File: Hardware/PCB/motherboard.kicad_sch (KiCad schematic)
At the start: 0 parts

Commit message: added stm32 to the project
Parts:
- added C8: 0.1 uF, symbol Device:C
- added JP1: Jumper, symbol Jumper:SolderJumper_2_Open
- added P1: USB_C_Plug_USB2.0, symbol Connector:USB_C_Plug_USB2.0
- added SW1: reset btn, symbol Switch:SW_Push
- added U4: STM32F303VCTx, Package_QFP:LQFP-100_14x14mm_P0.5mm, symbol MCU_ST_STM32F3:STM32F303VCTx
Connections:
- new net: C8.1, SW1.2, U4.14 (NRST)
- new net +3.3V: JP1.1 (A), U4.94 (BOOT0)
- new net GND: C8.2, JP1.2 (B), P1.A1 (GND), P1.A12 (GND), P1.B1 (GND), P1.B12 (GND), P1.SH (SHIELD), SW1.1, U4.20 (VSSA), U4.49 (VSS), U4.74 (VSS), U4.99 (VSS)
- new net USB_D+: P1.A6 (D+), U4.71 (PA12)
- new net USB_D-: P1.A7 (D-), U4.70 (PA11)
- new net VBUS: P1.A4 (VBUS), P1.A9 (VBUS), P1.B4 (VBUS), P1.B9 (VBUS)
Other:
- title: (none) -> STM32 mothersheet

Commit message: adding power management
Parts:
- removed P1: USB_C_Plug_USB2.0, symbol Connector:USB_C_Plug_USB2.0
- added C13, C14: 470n, symbol Device:C
- added C16, C17, C18, C3: 100n, symbol Device:C
- added C19, C21: 100n, Capacitor_SMD:C_0402_1005Metric, symbol Device:C
- added C2: 10u, symbol Device:C
- added C20: 4.7u, symbol Device:C
- added C4, C5: 22u, symbol Device:C
- added J1: USB4105-GF-A, Connector_USB:USB_C_Receptacle_GCT_USB4105-xx-A_16P_TopMnt_Horizontal, symbol Connector:USB_C_Receptacle_USB2.0_16P
- added L1: 3.9u, symbol Device:L
- added R14: 0R, symbol Device:R
- added R15, R16: 5K1, symbol Device:R
- added TP1: USB D1-, symbol Connector:TestPoint
- added TP2: USB D1+, symbol Connector:TestPoint
- added TP3: Vbus, symbol Connector:TestPoint
- added TP4: 3.3V, symbol Connector:TestPoint
- added U2: AP63203WU, Package_TO_SOT_SMD:TSOT-23-6, symbol Regulator_Switching:AP63203WU
- JP1: footprint (none) -> Jumper:SolderJumper-2_P1.3mm_Open_RoundedPad1.0x1.5mm
- renumbered C8 to C1, U4 to U1
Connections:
- net +3.3V: now also U1.100 (VDD), U1.21 (VREF+), U1.22 (VDDA), U1.28 (VDD), U1.50 (VDD), U1.75 (VDD), C16.1, C17.1, C18.1, C19.1, C20.1, C21.1, C4.1, C5.2, L1.2, TP4.1, U2.1 (FB)
- net GND: now also C13.2, C14.2, C16.2, C17.2, C18.2, C19.2, C2.2, C20.2, C21.2, C4.2, C5.1, J1.A1 (GND), J1.A12 (GND), J1.B1 (GND), J1.B12 (GND), J1.SH (SHIELD), R15.2, R16.2, U2.4 (GND)
- net USB_D+: now also J1.A6 (D+), J1.B6 (D+), TP2.1
- net USB_D-: now also J1.A7 (D-), J1.B7 (D-), TP1.1
- net VBUS: now also C13.1, C2.1, J1.A4 (VBUS), J1.A9 (VBUS), J1.B4 (VBUS), J1.B9 (VBUS), R14.2, TP3.1, U2.2 (EN), U2.3 (IN)
- new net: C3.1, U2.6 (BST)
- new net: C3.2, L1.1, U2.5 (SW)
- new net: J1.A5 (CC1), R15.1
- new net: J1.B5 (CC2), R16.1
- new net: C14.1, R14.1
- no-connect marks 0 -> 2
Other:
- note added: "Buck IC 5V->3.3V"
- note added: "PI filter"
- note added: "USB4105-GF-A"
- note added: "jlc link"
- note added: "must be connected to VDDA"
- note added: "voltage testpoints"

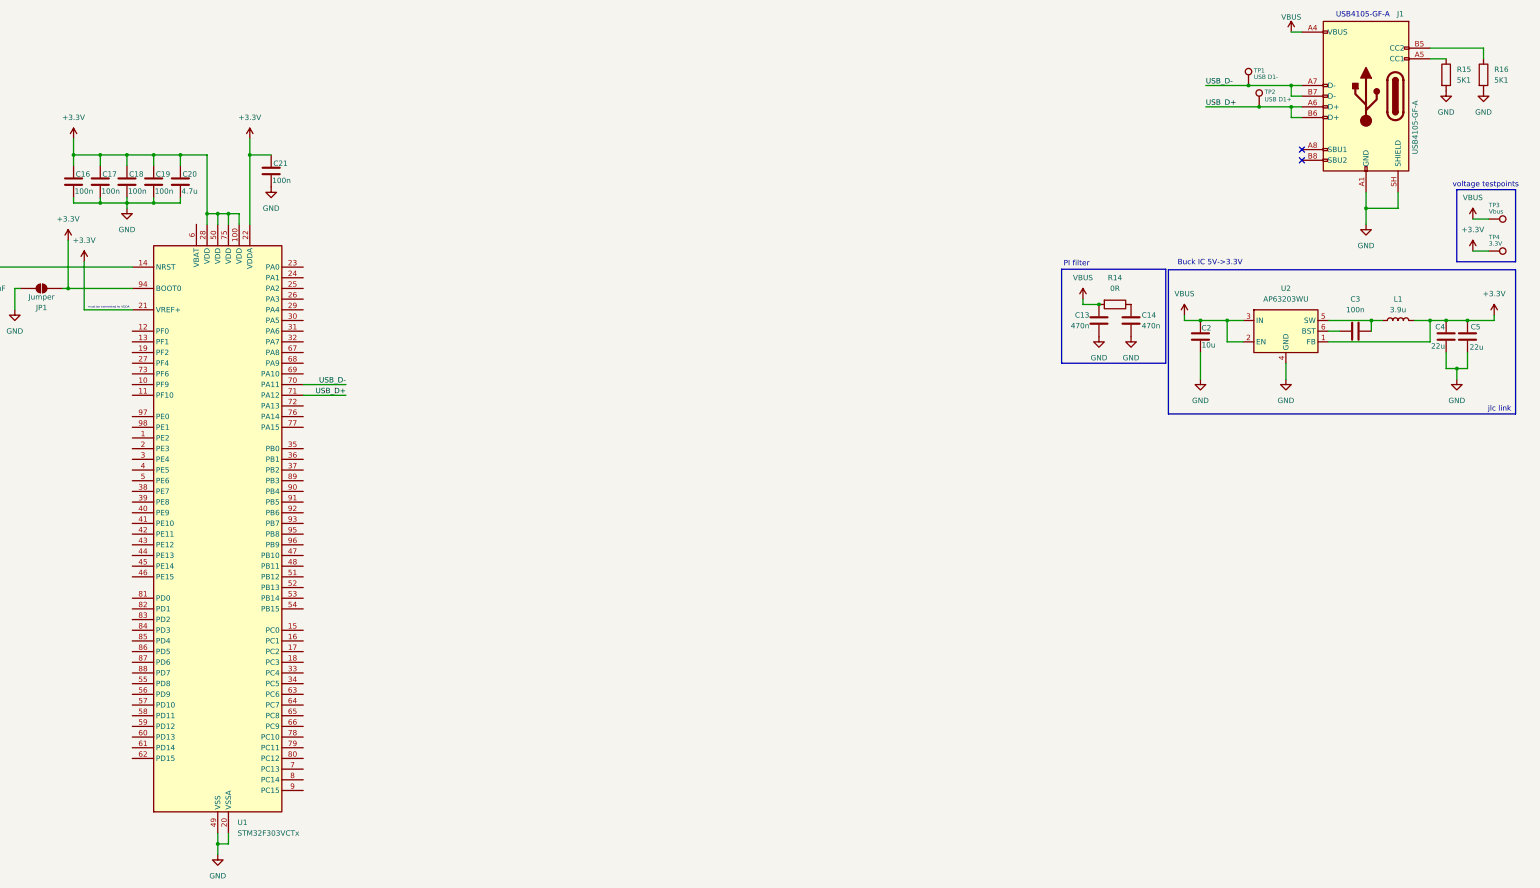
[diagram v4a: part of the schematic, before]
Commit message: added status LED's esd protection and new RGB symbol
Mass renumbering and library updates across KiCad schematics: updated many component Reference fields in Hardware/PCB/FM_reciever.kicad_sch and adjusted the project used_designators in Radiowekker.kicad_pro to match. Added a Device:LED symbol (with LED variants) to motherboard.kicad_sch and replaced the AP63203WU regulator symbol with a USBLC6-2SC6 power-protection symbol (updated footprint, datasheet, pins and graphics). Also added sym-lib-table and an RGB_leds symbol library. These changes keep designators consistent and introduce LED/ESD protection symbols for use in the PCB designs.
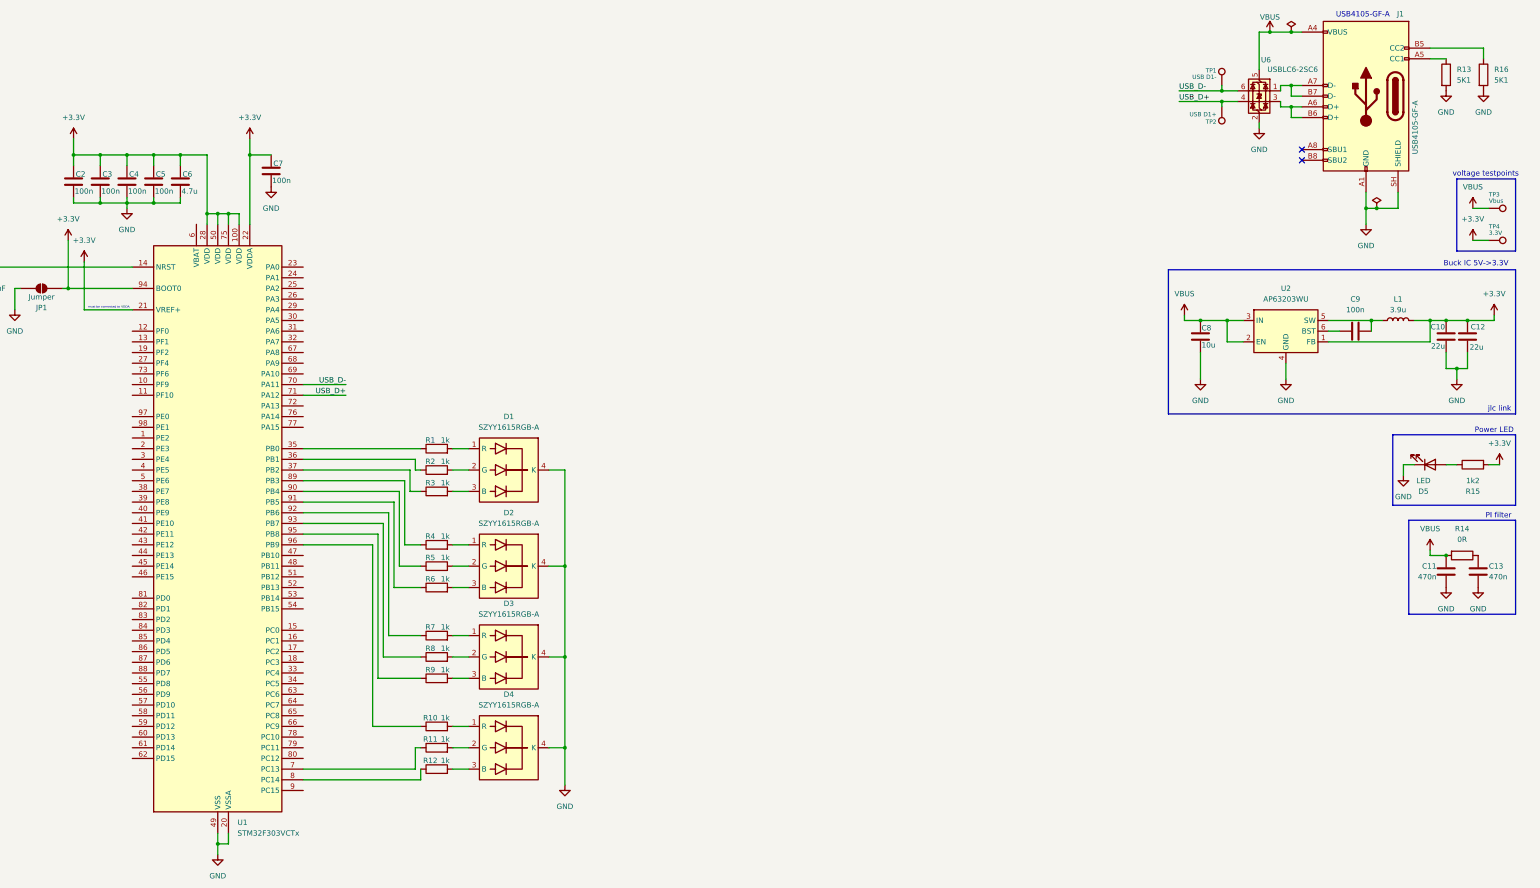
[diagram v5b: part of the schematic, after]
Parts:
- added D1, D2, D3, D4: SZYY1615RGB-A, symbol RGB_leds:SZYY1615RGB-A
- added D5: LED, symbol Device:LED
- added R1, R10, R11, R12, R2, R3, R4, R5, R6, R7, R8, R9: 1k, symbol Device:R
- added R15: 1k2, symbol Device:R
- added U6: USBLC6-2SC6, Package_TO_SOT_SMD:SOT-23-6, symbol Power_Protection:USBLC6-2SC6
- renumbered C4 to C10, C13 to C11, C5 to C12, C14 to C13, C16 to C2, C17 to C3, C18 to C4, C19 to C5, C20 to C6, C21 to C7, C2 to C8, C3 to C9, R15 to R13
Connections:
- net +3.3V: now also R15.2
- net GND: now also D1.4 (K), D2.4 (K), D3.4 (K), D4.4 (K), D5.1 (K), U6.2 (GND)
- net USB_D+: now also U6.4 (I/O2); no longer J1.A6 (D+), J1.B6 (D+)
- net USB_D-: now also U6.6 (I/O1); no longer J1.A7 (D-), J1.B7 (D-)
- net VBUS: now also U6.5 (VBUS)
- net at U1.35 (PB0): now also R1.1
- net at U1.36 (PB1): now also R2.1
- net at U1.37 (PB2): now also R3.1
- net at U1.7 (PC13): now also R11.1
- net at U1.8 (PC14): now also R12.1
- net at U1.89 (PB3): now also R4.1
- net at U1.90 (PB4): now also R5.1
- net at U1.91 (PB5): now also R6.1
- net at U1.92 (PB6): now also R7.1
- net at U1.93 (PB7): now also R8.1
- net at U1.95 (PB8): now also R9.1
- net at U1.96 (PB9): now also R10.1
- new net: D1.1 (R), R1.2
- new net: D3.2 (G), R8.2
- new net: D3.3 (B), R9.2
- new net: D1.2 (G), R2.2
- new net: D4.2 (G), R11.2
- new net: D3.1 (R), R7.2
- new net: D4.1 (R), R10.2
- new net: D4.3 (B), R12.2
- new net: D2.3 (B), R6.2
- new net: D2.1 (R), R4.2
- new net: D2.2 (G), R5.2
- new net: J1.A7 (D-), J1.B7 (D-), U6.1 (I/O1)
- new net: J1.A6 (D+), J1.B6 (D+), U6.3 (I/O2)
- new net: D1.3 (B), R3.2
- new net: D5.2 (A), R15.1
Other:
- note added: "Power LED"
- moved on the sheet: C11, C13, R14, TP1, TP2, TP3, TP4

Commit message: added UI
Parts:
- renumbered U6 to U2, U2 to U3
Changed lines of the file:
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@@
 		(dnp no)
 		(fields_autoplaced yes)
-		(property "Reference" "#PWR020"
+		(property "Reference" "#PWR021"
 			(at 544.83 163.83 0)
 			(hide yes)
@@
 			(project "Radiowekker"
 				(path "/d1c96533-fea5-409f-9018-c843faf96bf8/031f395c-467c-47af-acd6-d1b5a436666d"
-					(reference "#PWR020")
+					(reference "#PWR021")
 					(unit 1)
 				)
@@
 		(dnp no)
 		(fields_autoplaced yes)
-		(property "Reference" "#PWR026"
+		(property "Reference" "#PWR027"
 			(at 556.26 96.52 0)
 			(hide yes)
@@
 			(project "Radiowekker"
 				(path "/d1c96533-fea5-409f-9018-c843faf96bf8/031f395c-467c-47af-acd6-d1b5a436666d"
-					(reference "#PWR026")
+					(reference "#PWR027")
 					(unit 1)
 				)
@@
 		(dnp no)
 		(fields_autoplaced yes)
-		(property "Reference" "#PWR024"
+		(property "Reference" "#PWR025"
 			(at 552.45 163.83 0)
 			(hide yes)
@@
 			(project "Radiowekker"
 				(path "/d1c96533-fea5-409f-9018-c843faf96bf8/031f395c-467c-47af-acd6-d1b5a436666d"
-					(reference "#PWR024")
+					(reference "#PWR025")
 					(unit 1)
 				)
@@
 		(in_pos_files yes)
 		(dnp no)
-		(property "Reference" "#PWR014"
+		(property "Reference" "#PWR015"
 			(at 502.92 29.21 0)
 			(hide yes)
@@
 			(project "Radiowekker"
 				(path "/d1c96533-fea5-409f-9018-c843faf96bf8/031f395c-467c-47af-acd6-d1b5a436666d"
-					(reference "#PWR014")
+					(reference "#PWR015")
 					(unit 1)
 				)
@@
 		(dnp no)
 		(fields_autoplaced yes)
-		(property "Reference" "#PWR027"
+		(property "Reference" "#PWR028"
 			(at 557.53 132.08 0)
 			(hide yes)
@@
 			(project "Radiowekker"
 				(path "/d1c96533-fea5-409f-9018-c843faf96bf8/031f395c-467c-47af-acd6-d1b5a436666d"
-					(reference "#PWR027")
+					(reference "#PWR028")
 					(unit 1)
 				)
@@
 		(dnp no)
 		(fields_autoplaced yes)
-		(property "Reference" "#PWR016"
+		(property "Reference" "#PWR017"
 			(at 525.78 77.47 0)
 			(hide yes)
@@
 			(project "Radiowekker"
 				(path "/d1c96533-fea5-409f-9018-c843faf96bf8/031f395c-467c-47af-acd6-d1b5a436666d"
-					(reference "#PWR016")
+					(reference "#PWR017")
 					(unit 1)
 				)
@@
 		(dnp no)
 		(fields_autoplaced yes)
-		(property "Reference" "#PWR018"
+		(property "Reference" "#PWR019"
 			(at 541.02 152.4 0)
 			(hide yes)
@@
 			(project "Radiowekker"
 				(path "/d1c96533-fea5-409f-9018-c843faf96bf8/031f395c-467c-47af-acd6-d1b5a436666d"
-					(reference "#PWR018")
+					(reference "#PWR019")
 					(unit 1)
 				)
@@
 		(in_pos_files yes)
 		(dnp no)
-		(property "Reference" "U6"
+		(property "Reference" "U2"
 			(at 503.174 32.004 0)
 			(show_name no)
@@
 			(project "Radiowekker"
 				(path "/d1c96533-fea5-409f-9018-c843faf96bf8/031f395c-467c-47af-acd6-d1b5a436666d"
-					(reference "U6")
+					(reference "U2")
 					(unit 1)
 				)
@@
 		(dnp no)
 		(fields_autoplaced yes)
-		(property "Reference" "#PWR025"
+		(property "Reference" "#PWR026"
 			(at 553.72 45.72 0)
 			(hide yes)
@@
 			(project "Radiowekker"
 				(path "/d1c96533-fea5-409f-9018-c843faf96bf8/031f395c-467c-47af-acd6-d1b5a436666d"
-					(reference "#PWR025")
+					(reference "#PWR026")
 					(unit 1)
 				)
@@
 		(dnp no)
 		(fields_autoplaced yes)
-		(property "Reference" "#PWR022"
+		(property "Reference" "#PWR023"
 			(at 551.18 71.12 0)
 			(hide yes)
@@
 			(project "Radiowekker"
 				(path "/d1c96533-fea5-409f-9018-c843faf96bf8/031f395c-467c-47af-acd6-d1b5a436666d"
-					(reference "#PWR022")
+					(reference "#PWR023")
 					(unit 1)
 				)
@@
 		(dnp no)
 		(fields_autoplaced yes)
-		(property "Reference" "#PWR019"
+		(property "Reference" "#PWR020"
 			(at 544.83 45.72 0)
 			(hide yes)
@@
 			(project "Radiowekker"
 				(path "/d1c96533-fea5-409f-9018-c843faf96bf8/031f395c-467c-47af-acd6-d1b5a436666d"
-					(reference "#PWR019")
+					(reference "#PWR020")
 					(unit 1)
 				)
@@
 		(dnp no)
 		(fields_autoplaced yes)
-		(property "Reference" "#PWR023"
+		(property "Reference" "#PWR024"
 			(at 551.18 78.74 0)
 			(hide yes)
@@
 			(project "Radiowekker"
 				(path "/d1c96533-fea5-409f-9018-c843faf96bf8/031f395c-467c-47af-acd6-d1b5a436666d"
-					(reference "#PWR023")
+					(reference "#PWR024")
 					(unit 1)
 				)
@@
 		(dnp no)
 		(fields_autoplaced yes)
-		(property "Reference" "#PWR041"
+		(property "Reference" "#PWR014"
 			(at 500.38 54.61 0)
 			(hide yes)
@@
 			(project "Radiowekker"
 				(path "/d1c96533-fea5-409f-9018-c843faf96bf8/031f395c-467c-47af-acd6-d1b5a436666d"
-					(reference "#PWR041")
+					(reference "#PWR014")
 					(unit 1)
 				)
@@
 		(dnp no)
 		(fields_autoplaced yes)
-		(property "Reference" "#PWR021"
+		(property "Reference" "#PWR022"
 			(at 547.37 114.3 0)
 			(hide yes)
@@
 			(project "Radiowekker"
 				(path "/d1c96533-fea5-409f-9018-c843faf96bf8/031f395c-467c-47af-acd6-d1b5a436666d"
-					(reference "#PWR021")
+					(reference "#PWR022")
 					(unit 1)
 				)
@@
 		(dnp no)
 		(fields_autoplaced yes)
-		(property "Reference" "#PWR017"
+		(property "Reference" "#PWR018"
 			(at 534.67 137.16 0)
 			(hide yes)
@@
 			(project "Radiowekker"
 				(path "/d1c96533-fea5-409f-9018-c843faf96bf8/031f395c-467c-47af-acd6-d1b5a436666d"
-					(reference "#PWR017")
+					(reference "#PWR018")
 					(unit 1)
 				)
@@
 		(dnp no)
 		(fields_autoplaced yes)
-		(property "Reference" "U2"
+		(property "Reference" "U3"
 			(at 506.73 86.36 0)
 			(show_name no)
@@
 			(project "Radiowekker"
 				(path "/d1c96533-fea5-409f-9018-c843faf96bf8/031f395c-467c-47af-acd6-d1b5a436666d"
-					(reference "U2")
+					(reference "U3")
 					(unit 1)
 				)
@@
 		(dnp no)
 		(fields_autoplaced yes)
-		(property "Reference" "#PWR015"
+		(property "Reference" "#PWR016"
 			(at 506.73 114.3 0)
 			(hide yes)
@@
 			(project "Radiowekker"
 				(path "/d1c96533-fea5-409f-9018-c843faf96bf8/031f395c-467c-47af-acd6-d1b5a436666d"
-					(reference "#PWR015")
+					(reference "#PWR016")
 					(unit 1)
 				)

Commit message: added buttons
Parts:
- removed C10, C12: 22u, symbol Device:C
- removed C11, C13: 470n, symbol Device:C
- removed C8: 10u, symbol Device:C
- removed C9: 100n, symbol Device:C
- removed D5: LED, symbol Device:LED
- removed L1: 3.9u, symbol Device:L
- removed R14: 0R, symbol Device:R
- removed R15: 1k2, symbol Device:R
- removed TP3: Vbus, symbol Connector:TestPoint
- removed TP4: 3.3V, symbol Connector:TestPoint
- removed U3: AP63203WU, Package_TO_SOT_SMD:TSOT-23-6, symbol Regulator_Switching:AP63203WU
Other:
- note added: "STM32 IC"
- note added: "USB C connector"
- note removed: "Buck IC 5V->3.3V"
- note removed: "PI filter"
- note removed: "Power LED"
- note removed: "jlc link"
- note removed: "voltage testpoints"
- moved on the sheet: C1, C2, C3, C4, C5, C6, C7, D1, D2, D3, D4, J1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

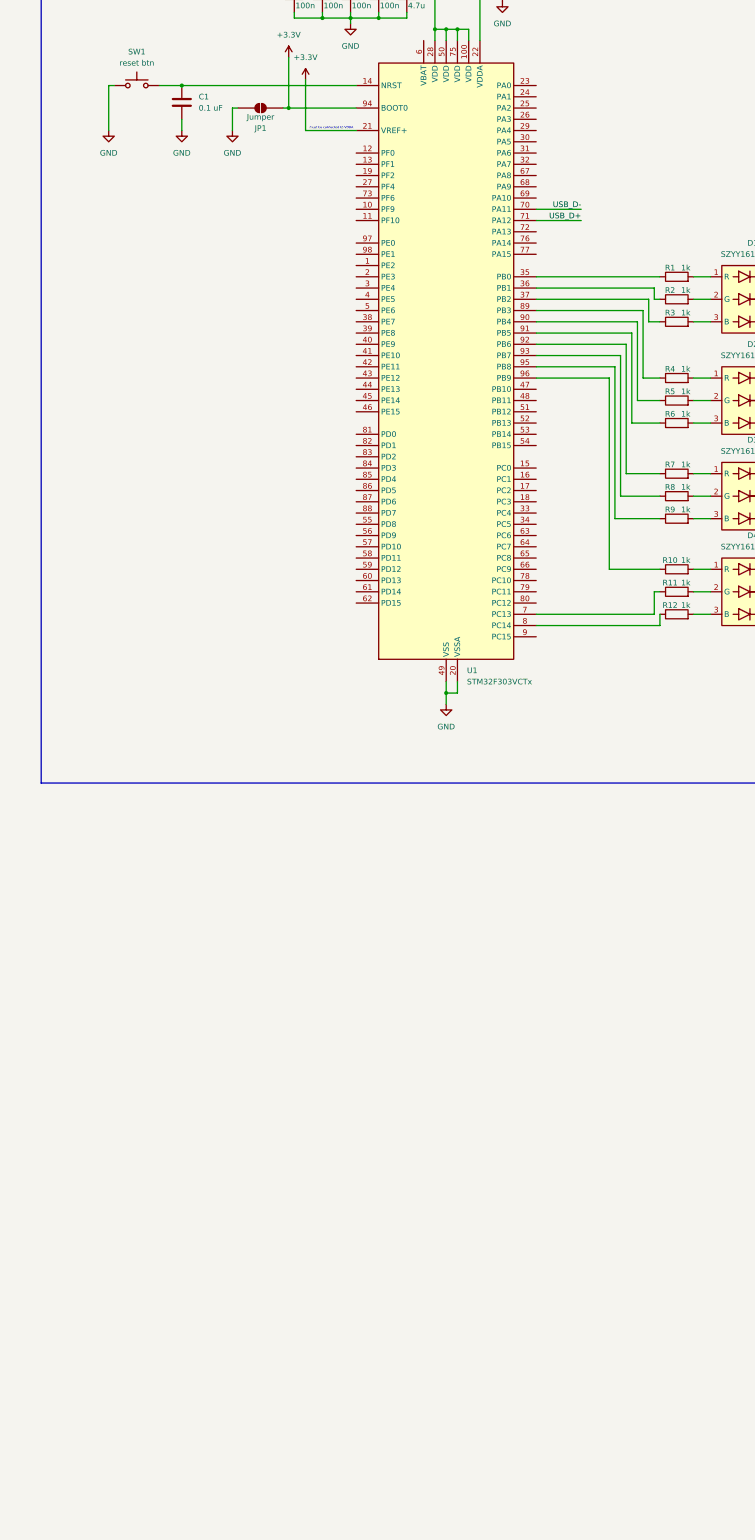
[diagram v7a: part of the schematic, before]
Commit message: added connection hierachie pins
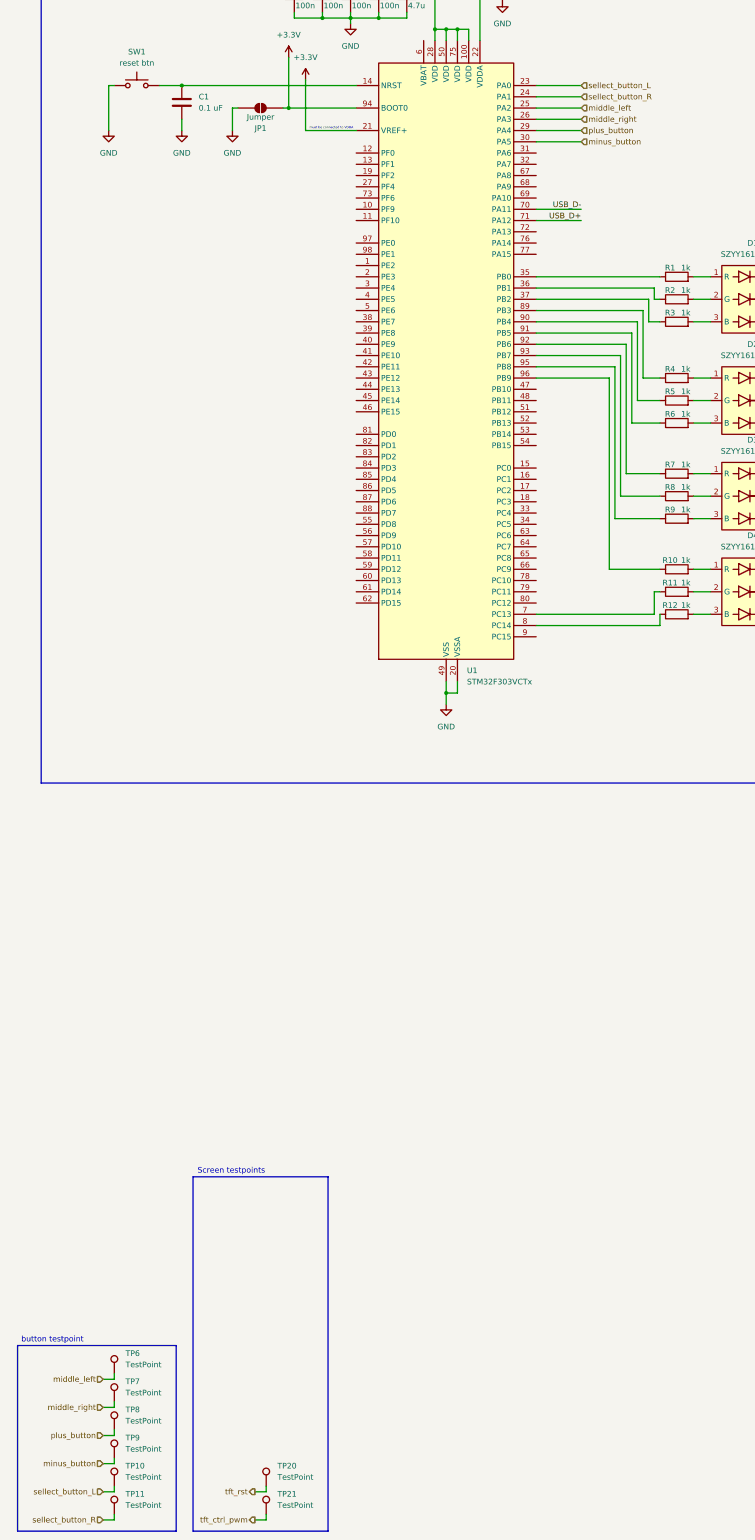
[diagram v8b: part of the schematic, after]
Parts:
- added TP10, TP11, TP20, TP21, TP6, TP7, TP8, TP9: TestPoint, symbol Connector:TestPoint
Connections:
- net sellect_button_L: now reaches U1.23 (PA0)
- net sellect_button_L: now also TP10.1
- net sellect_button_R: now reaches U1.24 (PA1)
- net sellect_button_R: now also TP11.1
- net middle_left: now reaches U1.25 (PA2)
- net middle_left: now also TP6.1
- net middle_right: now reaches U1.26 (PA3)
- net middle_right: now also TP7.1
- net plus_button: now reaches U1.29 (PA4)
- net plus_button: now also TP8.1
- net minus_button: now reaches U1.30 (PA5)
- net minus_button: now also TP9.1
- new net tft_ctrl_pwm: TP21.1
- new net tft_rst: TP20.1
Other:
- note added: "Screen testpoints"
- note added: "button testpoint"
